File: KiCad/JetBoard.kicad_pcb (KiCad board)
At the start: 4 copper layers, 42.6 x 53.2 mm, 86 parts, among them J1 USB_C_Receptacle_USB2.0_16P, J2 Conn_01x02_Socket, SW1 SW_Push, U1 RP2040, U10 STM8S001J3M, U11 RT5715GQW, U12 BQ25185DLHR, U13 TPS2116DRL, U14 TPS2116DRL, U15 TPS2552DRVR, U16 ATGM336H-5N31, U2 W25Q16JVUXIQ, U4 Si5351A-B-GT, U5 TLV61070ADBVR, U7 TPS7A0533PDBZ, U9 TPS2552DRVR, X2 X1G0042110003_C3013793, Y1 12.000MHz-ABM8-272-T3

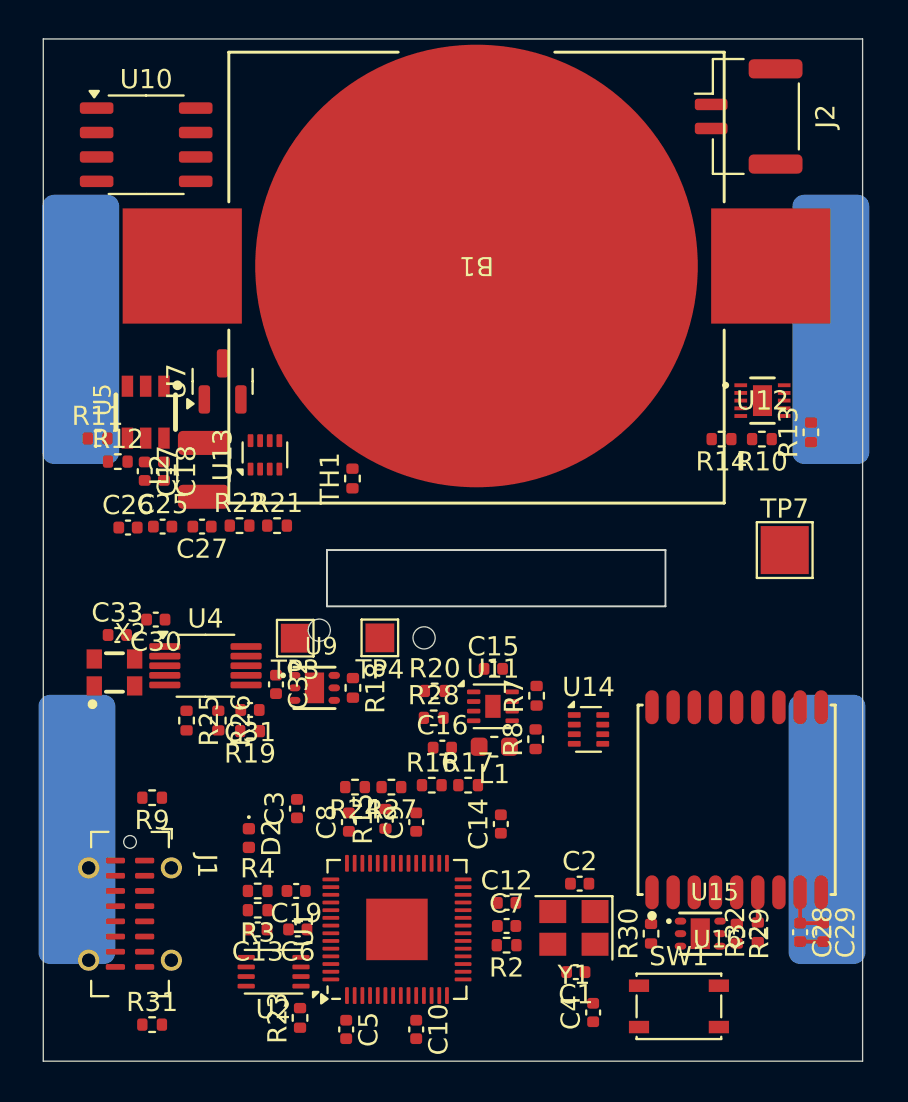
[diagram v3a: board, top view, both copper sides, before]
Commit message: 3D model fixes and change to 3.0V buck
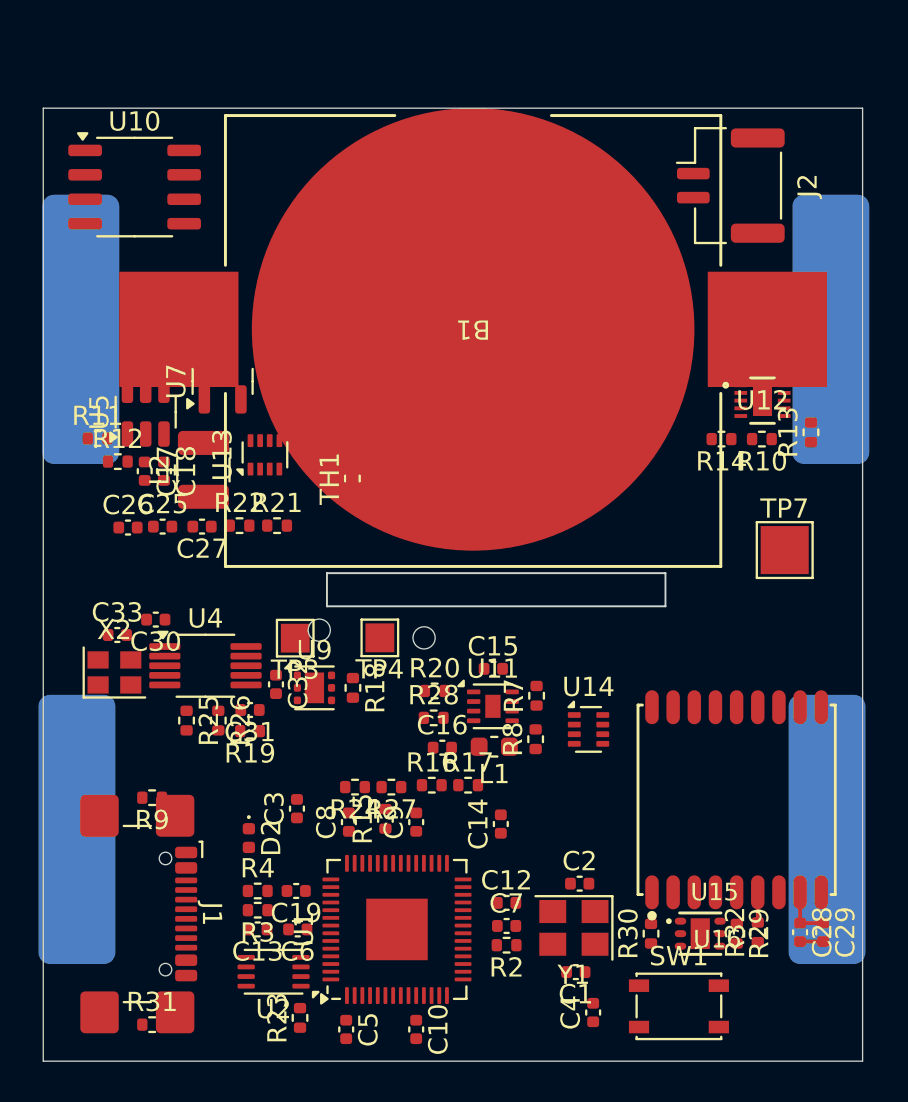
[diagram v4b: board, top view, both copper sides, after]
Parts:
- J1: footprint Connector_USB:USB_C_Receptacle_G-Switch_GT-USB-7051x -> Connector_USB:USB_C_Receptacle_GCT_USB4110
- R7: value 284.3k -> 221k
- U10: value STM8S001J3M -> STM8S050
- U5: footprint JetBoard:SOT-23-6_L2.9-W1.6-P0.95-LS2.8-BR -> Package_TO_SOT_SMD:SOT-23-6
- U7: value TPS7A0533PDBZ -> TPS7A0530PDBZ
- U9: footprint JetBoard:WSON-6_L2.0-W2.0-P0.65-TL-EP -> Package_SON:WSON-6-1EP_2x2mm_P0.65mm_EP1x1.6mm
- X2: footprint JetBoard:OSC-SMD_4P-L2.5-W2.0-BL_X1G0042110003 -> Oscillator:Oscillator_SMD_SeikoEpson_SG210-4Pin_2.5x2.0mm
- moved J2 3.71 mm to (165.6, 79.9)
- moved B1 3.30 mm to (152.2, 88.0)
- moved U10 2.28 mm to (134.6, 80.0)
- moved J1 0.76 mm to (133.6, 117.8)
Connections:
- net +3V3_GNSS renamed +3V0_GNSS
- net +3V3_WSPR renamed +3V0_WSPR
- net +V_BAT_3V3 renamed +V_BAT_3V0
- net /gnss/3V3_GNSS_EN# renamed /gnss/3V0_GNSS_EN#
- net /rp2040/3V3_GNSS_EN# renamed /rp2040/3V0_GNSS_EN#
- net /rp2040/3V3_WSPR_EN# renamed /rp2040/3V0_WSPR_EN#
- net /wspr transmitter/3V3_WSPR_EN# renamed /wspr transmitter/3V0_WSPR_EN#
- net VBAT_3V3 renamed VBAT_3V0
- net V_BAT_3V3 renamed V_BAT_3V0
- C10 pad 1: +3V3 -> +3V0
- C14 pad 1: +3V3 -> +3V0
- C15 pad 1: +3V3 -> +3V0
- C3 pad 1: +3V3 -> +3V0
- C4 pad 1: +3V3 -> +3V0
- C5 pad 1: +3V3 -> +3V0
- C6 pad 1: +3V3 -> +3V0
- C7 pad 1: +3V3 -> +3V0
- C8 pad 1: +3V3 -> +3V0
- C9 pad 1: +3V3 -> +3V0
- L1 pad 2: +3V3 -> +3V0
- R18 pad 1: +3V3 -> +3V0
- R20 pad 1: /3V3 Buck/3V3_DCDC_EN -> /3V0_DCDC_EN
- R21 pad 1: /rp2040/STM8_SDA -> /STM8_SCL
- R21 pad 2: +3V3 -> +3V0
- R22 pad 1: /rp2040/STM8_SCL -> /STM8_SDA
- R22 pad 2: +3V3 -> +3V0
- R25 pad 2: +3V3 -> +3V0
- R26 pad 2: +3V3 -> +3V0
- R28 pad 2: +3V3 -> +3V0
- R29 pad 1: +3V3 -> +3V0
- R30 pad 2: +3V3 -> +3V0
- U1 pad 1: +3V3 -> +3V0
- U1 pad 10: +3V3 -> +3V0
- U1 pad 16: /rp2040/STM8_SDA -> /STM8_SWIM
- U1 pad 17: /rp2040/STM8_SDA -> /STM8_SCL
- U1 pad 18: /rp2040/STM8_SCL -> /STM8_SDA
- U1 pad 22: +3V3 -> +3V0
- U1 pad 33: +3V3 -> +3V0
- U1 pad 42: +3V3 -> +3V0
- U1 pad 43: +3V3 -> +3V0
- U1 pad 44: +3V3 -> +3V0
- U1 pad 48: +3V3 -> +3V0
- U1 pad 49: +3V3 -> +3V0
- U10 pad 5: /alarm clock/STM8_SCL -> /STM8_SCL
- U10 pad 6: /alarm clock/STM8_SDA -> /STM8_SDA
- U10 pad 7: /alarm clock/3V3_DCDC_EN# -> /3V0_DCDC_EN
- U10 pad 8: /alarm clock/STM8_SWIM -> /STM8_SWIM
- U11 pad 1: /3V3 Buck/3V3_DCDC_EN -> /3V0_DCDC_EN
- U11 pad 5: +3V3 -> +3V0
- U15 pad 6: +3V3 -> +3V0
- U9 pad 6: +3V3 -> +3V0
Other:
- board size 42.6 x 53.2 mm -> 42.6 x 49.5 mm

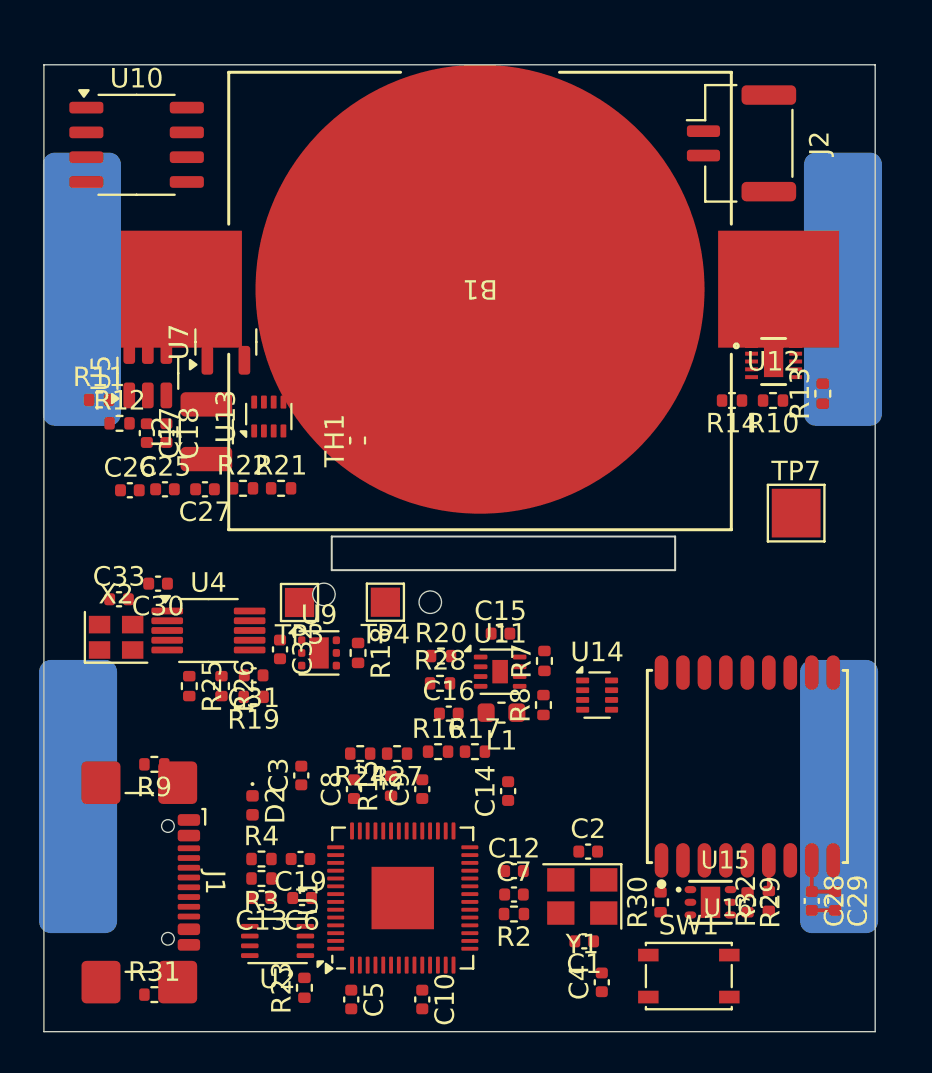
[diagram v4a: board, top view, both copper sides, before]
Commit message: Schematic changes
- Changed to STM8L050
- Changed to SPI interface for STM8 bootloader
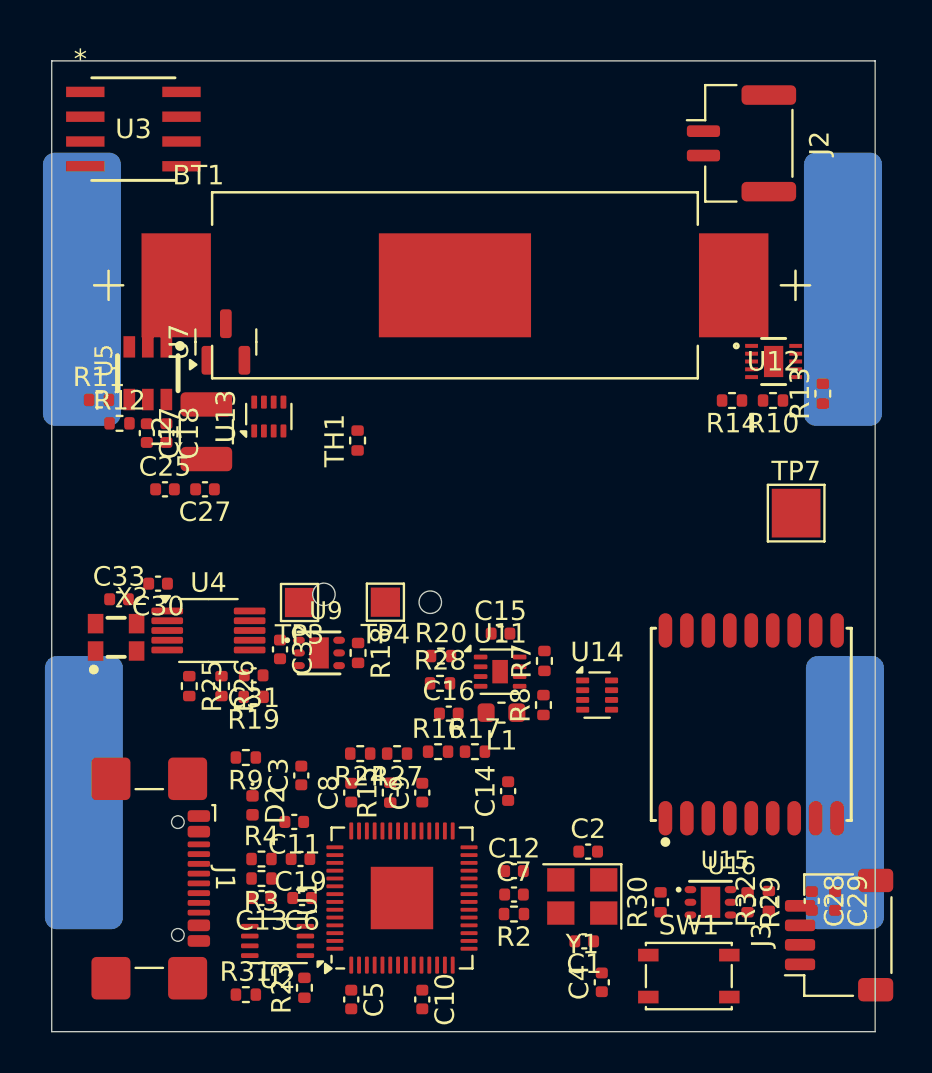
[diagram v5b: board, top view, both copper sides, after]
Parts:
- removed B1: BAT-HLD-006-SMT, JetBoard:BAT-HLD-006-SMT_LNX
- removed C26: 100nF, Capacitor_SMD:C_0402_1005Metric
- removed R21, R22: 5.1k, Resistor_SMD:R_0402_1005Metric
- removed U10: STM8S050, Package_SO:SO-8_3.9x4.9mm_P1.27mm
- added BT1: BC-2013, JetBoard:BAT_BC-2013, F.Cu at (150.9, 87.2)
- added C11: 100nF, Capacitor_SMD:C_0402_1005Metric, F.Cu at (142.7, 114.7)
- added J3: Conn_01x04, Connector_JST:JST_SH_SM04B-SRSS-TB_1x04-1MP_P1.00mm_Horizontal, F.Cu at (170.6, 120.5)
- added U3: STM8L050J3M3, JetBoard:SOD8N_4P9X6, F.Cu at (134.4, 79.2)
- U5: footprint Package_TO_SOT_SMD:SOT-23-6 -> JetBoard:SOT-23-6_L2.9-W1.6-P0.95-LS2.8-BR
- U9: footprint Package_SON:WSON-6-1EP_2x2mm_P0.65mm_EP1x1.6mm -> JetBoard:WSON-6_L2.0-W2.0-P0.65-TL-EP
- X2: footprint Oscillator:Oscillator_SMD_SeikoEpson_SG210-4Pin_2.5x2.0mm -> JetBoard:OSC-SMD_4P-L2.5-W2.0-BL_X1G0042110003
- moved R9 4.70 mm to (140.2, 111.4)
- moved R31 4.69 mm to (140.2, 123.5)
- moved U16 2.17 mm to (166.1, 109.7)
- moved J1 0.55 mm to (134.1, 117.6)
- moved SC2 0.36 mm to (150.9, 113.2)
- moved R15 0.35 mm to (147.6, 113.2)
- moved C8 0.23 mm to (145.6, 113.2)
- moved C9 0.18 mm to (149.2, 113.2)
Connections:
- net +3.3V_WSPR renamed +3.0V_WSPR
- R18 pad 2: /wspr transmitter/3V0_WSPR_EN# -> /3V0_WSPR_EN#
- R25 pad 1: /rp2040/SI5351_SDA -> /SCL
- R26 pad 1: /rp2040/SI5351_SCL -> /SI5351_SCL
- R32 pad 1: +V_BAT_3V0 -> VBAT_3V0
- R32 pad 2: VBAT_3V0 -> Net-(U16-VBAT)
- U1 pad 11: /rp2040/GNSS_UART_RX -> /gnss/GNSS_UART_RX
- U1 pad 12: /rp2040/GNSS_UART_TX -> /gnss/GNSS_UART_TX
- U1 pad 16: /STM8_SWIM -> /STM8_SPI_CLK
- U1 pad 17: /STM8_SCL -> /STM8_SPI_MISO
- U1 pad 18: /STM8_SDA -> /STM8_SPI_MOSI
- U1 pad 26: /rp2040/PI_RUN -> /PI_RUN
- U1 pad 4: /rp2040/3V0_GNSS_EN# -> /gnss/3V0_GNSS_EN#
- U1 pad 40: /rp2040/3V0_WSPR_EN# -> /3V0_WSPR_EN#
- U1 pad 43: +3V0 -> Net-(U1-ADC_AVDD)
- U1 pad 6: /rp2040/SI5351_SDA -> /SCL
- U1 pad 7: /rp2040/SI5351_SCL -> /SI5351_SCL
- U16 pad 6: VBAT_3V0 -> Net-(U16-VBAT)
- U16 pad 9: /gnss/GNSS_RESET# -> /rp2040/GPIO_6
- U4 pad 4: /wspr transmitter/SCL -> /SCL
- U4 pad 5: /wspr transmitter/SDA -> /SI5351_SCL
- U9 pad 4: /wspr transmitter/3V0_WSPR_EN# -> /3V0_WSPR_EN#
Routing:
- net +3V0_GNSS: track 2.80 -> 0.00 mm
- net VBAT_3V0: track 1.57 -> 0.00 mm
- net GND: track 1.20 -> 0.00 mm
- added copper zone on In1.Cu, net GND
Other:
- board size 42.6 x 49.5 mm -> 42.2 x 49.8 mm

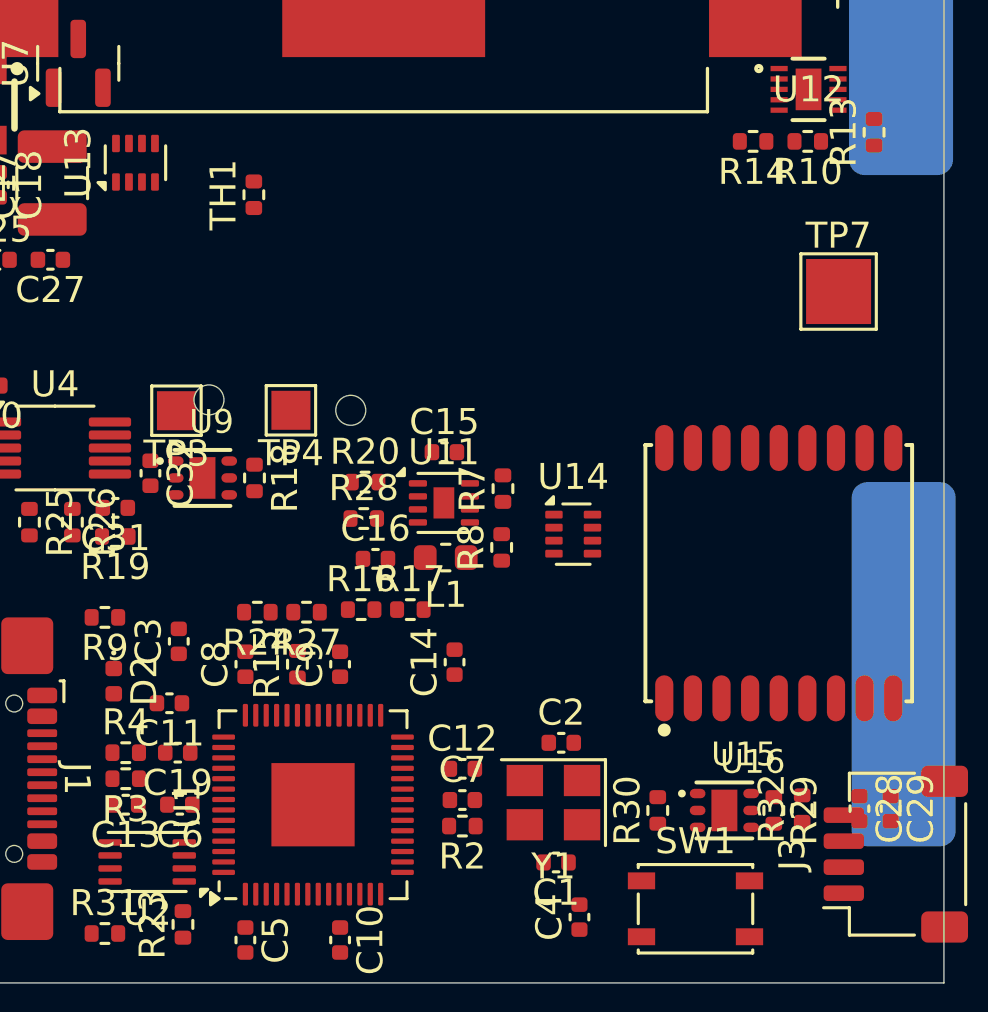
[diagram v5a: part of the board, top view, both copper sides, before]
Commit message: Clean up ERC errors
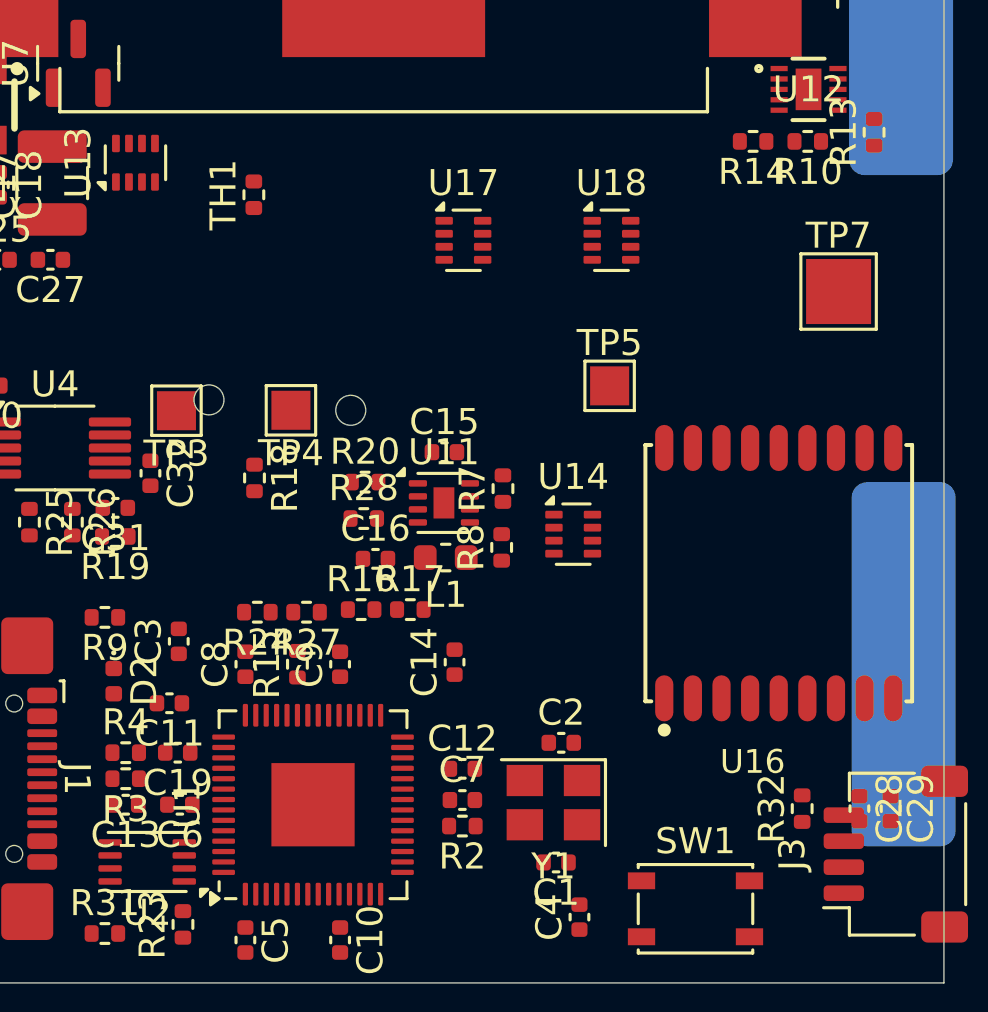
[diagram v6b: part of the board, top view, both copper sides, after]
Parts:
- removed R29: 10k, Resistor_SMD:R_0402_1005Metric
- removed R30: NS, Resistor_SMD:R_0402_1005Metric
- removed U15, U9: TPS2552DRVR, JetBoard:WSON-6_L2.0-W2.0-P0.65-TL-EP
- added TP5: TestPoint, TestPoint:TestPoint_Pad_1.5x1.5mm, F.Cu at (159.6, 102.5)
- added U17: TPS2116DRL, Package_TO_SOT_SMD:SOT-583-8, F.Cu at (154.0, 96.9)
- added U18: TPS2116DRL, Package_TO_SOT_SMD:SOT-583-8, F.Cu at (159.7, 96.9)
- R19: value NS -> 10k
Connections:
- C30 pad 1: +3.0V_WSPR -> +3V0_WSPR
- R14 pad 2: /battery/CHARGE_EN# -> /CHARGE_EN#
- R18 pad 1: +3V0 -> /3V0_WSPR_EN#
- R18 pad 2: /3V0_WSPR_EN# -> +3V0
- R19 pad 1: Net-(U9-ILIM) -> /gnss/3V0_GNSS_EN#
- R19 pad 2: GND -> +3V0
- R7 pad 2: +3.3V -> +3V0
- U12 pad 10: USB_VBUS -> V_IN
- U12 pad 4: /battery/CHARGE_EN# -> /CHARGE_EN#
- U14 pad 2: V_SYS -> V_IN
- U14 pad 7: V_SYS -> V_IN
- U3 pad 2: unconnected-(U3-PA3-Pad2) -> /CHARGE_EN#
- U3 pad 8: /alarm clock/STM8_UART_TX -> /STM8_UART_TX
- X2 pad 4: +3.0V_WSPR -> +3V0_WSPR

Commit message: Mods
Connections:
- net /3V0_WSPR_EN# renamed /WSPR.~{PWR_EN}
- net /CHARGE_EN# renamed /~{CHARGE_EN}
- net /STM8_SPI_CLK renamed /STM8.SPI.CLK
- net /STM8_SPI_MISO renamed /STM8.SPI.MISO
- net /STM8_SPI_MOSI renamed /STM8.SPI.MOSI
- net /gnss/3V0_GNSS_EN# renamed /GNSS.3V0_EN
- net /gnss/GNSS_UART_RX renamed /GNSS.UART_RX
- net /gnss/GNSS_UART_TX renamed /GNSS.UART_TX
- net /rp2040/GPIO_6 renamed /GNSS.~{RESET}
- net /rp2040/QSPI_CLK renamed /rp2040/QSPI.CLK
- net /rp2040/QSPI_SD0 renamed /rp2040/QSPI.SD0
- net /rp2040/QSPI_SD1 renamed /rp2040/QSPI.SD1
- net /rp2040/QSPI_SD2 renamed /rp2040/QSPI.SD2
- net /rp2040/QSPI_SD3 renamed /rp2040/QSPI.SD3
- net /rp2040/QSPI_SS renamed /rp2040/QSPI.SS
- R25 pad 1: /SCL -> /WSPR.SCL
- R25 pad 2: +3V0 -> +3V0_WSPR
- R26 pad 1: /SI5351_SCL -> /WSPR.SDA
- R26 pad 2: +3V0 -> +3V0_WSPR
- R32 pad 1: VBAT_3V0 -> V_BAT_3V0
- U1 pad 6: /SCL -> /WSPR.SDA
- U1 pad 7: /SI5351_SCL -> /WSPR.SCL
- U2 pad 8: +3V3 -> +3V0
- U4 pad 1: +3.0V_WSPR -> +3V0_WSPR
- U4 pad 4: /SCL -> /WSPR.SCL
- U4 pad 5: /SI5351_SCL -> /WSPR.SDA
- U4 pad 7: +3.0V_WSPR -> +3V0_WSPR
